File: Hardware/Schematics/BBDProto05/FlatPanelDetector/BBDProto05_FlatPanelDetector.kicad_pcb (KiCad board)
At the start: 2 copper layers, 170 x 110 mm, 124 parts, among them P01-01A1 VIA_06MM, P01-01B1 VIA_06MM, P01-02A1 VIA_06MM, P01-02B1 VIA_06MM, P01-03A1 VIA_06MM, P01-03B1 VIA_06MM, P01-04A1 VIA_06MM, P01-04B1 VIA_06MM, P01-05A1 VIA_06MM, P01-05B1 VIA_06MM, P01-06A1 VIA_06MM, P01-06B1 VIA_06MM, P02-01A1 VIA_06MM, P02-01B1 VIA_06MM, P02-02A1 VIA_06MM, P02-02B1 VIA_06MM, P02-03A1 VIA_06MM, P02-03B1 VIA_06MM, P02-04A1 VIA_06MM, P02-04B1 VIA_06MM, P02-05A1 VIA_06MM, P02-05B1 VIA_06MM, P02-06A1 VIA_06MM, P02-06B1 VIA_06MM, P03-01A1 VIA_06MM, P03-01B1 VIA_06MM, P03-02A1 VIA_06MM, P03-02B1 VIA_06MM, P03-03A1 VIA_06MM, P03-03B1 VIA_06MM, P03-04A1 VIA_06MM, P03-04B1 VIA_06MM, P03-05A1 VIA_06MM, P03-05B1 VIA_06MM, P03-06A1 VIA_06MM, P03-06B1 VIA_06MM, P04-01A1 VIA_06MM, P04-01B1 VIA_06MM, P04-02A1 VIA_06MM, P04-02B1 VIA_06MM, P04-03A1 VIA_06MM, P04-03B1 VIA_06MM, P04-04A1 VIA_06MM, P04-04B1 VIA_06MM, P04-05A1 VIA_06MM, P04-05B1 VIA_06MM, P04-06A1 VIA_06MM, P04-06B1 VIA_06MM, P05-01A1 VIA_06MM, P05-01B1 VIA_06MM, P05-02A1 VIA_06MM, P05-02B1 VIA_06MM, P05-03A1 VIA_06MM, P05-03B1 VIA_06MM, P05-04A1 VIA_06MM, P05-04B1 VIA_06MM, P05-05A1 VIA_06MM, P05-05B1 VIA_06MM, P05-06A1 VIA_06MM, P05-06B1 VIA_06MM, P06-01A1 VIA_06MM, P06-01B1 VIA_06MM, P06-02A1 VIA_06MM, P06-02B1 VIA_06MM, P06-03A1 VIA_06MM, P06-03B1 VIA_06MM, P06-04A1 VIA_06MM, P06-04B1 VIA_06MM, P06-05A1 VIA_06MM, P06-05B1 VIA_06MM, P06-06A1 VIA_06MM, P06-06B1 VIA_06MM, P07-01A1 VIA_06MM, P07-01B1 VIA_06MM, P07-02A1 VIA_06MM, P07-02B1 VIA_06MM, P07-03A1 VIA_06MM, P07-03B1 VIA_06MM, P07-04A1 VIA_06MM, P07-04B1 VIA_06MM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

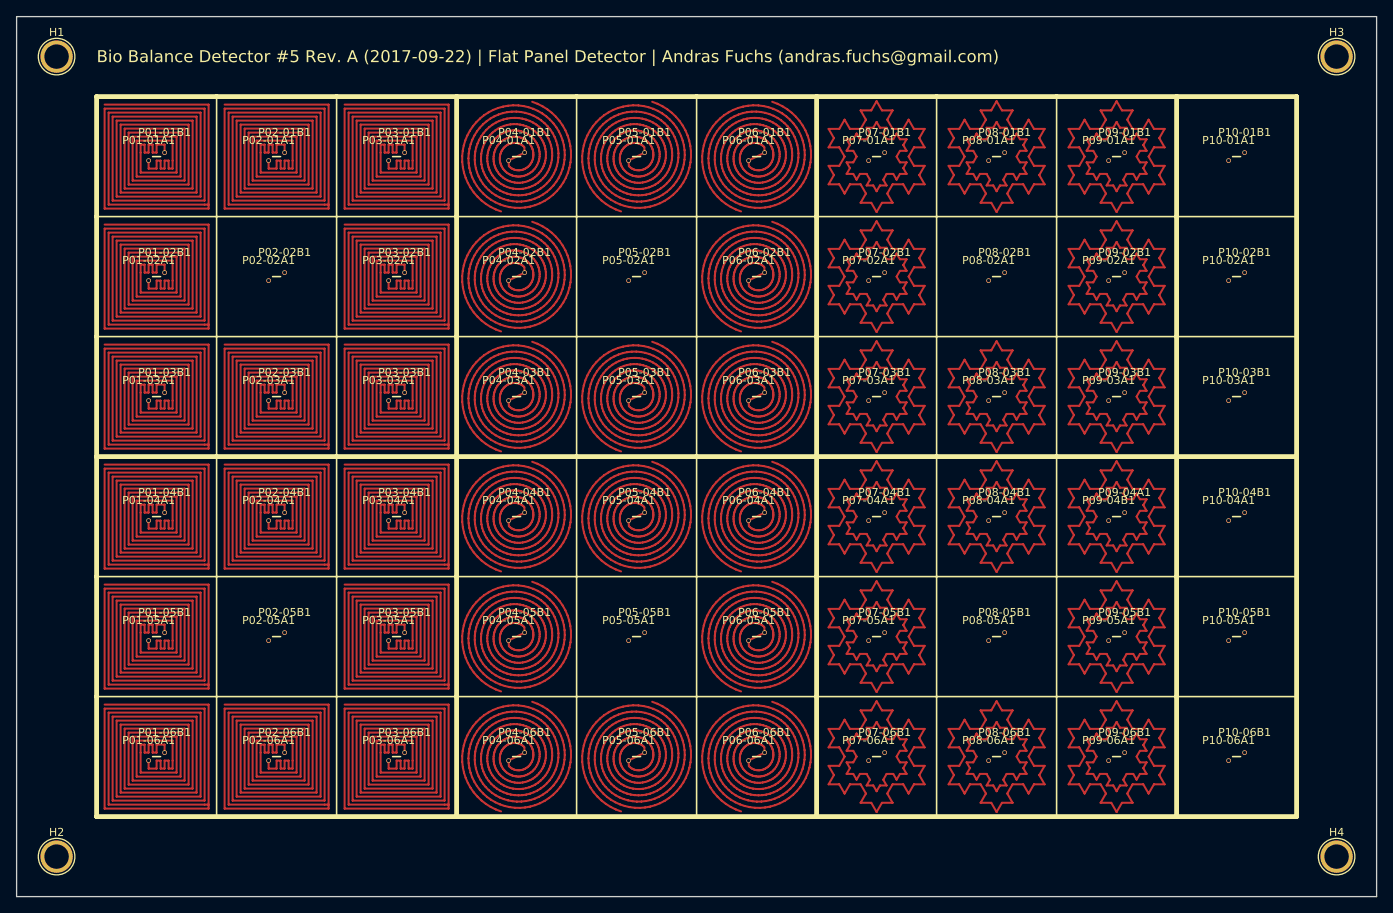
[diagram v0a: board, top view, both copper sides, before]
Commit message: FlatPanelDetector and its generator
FlatPanelDetector and its generator
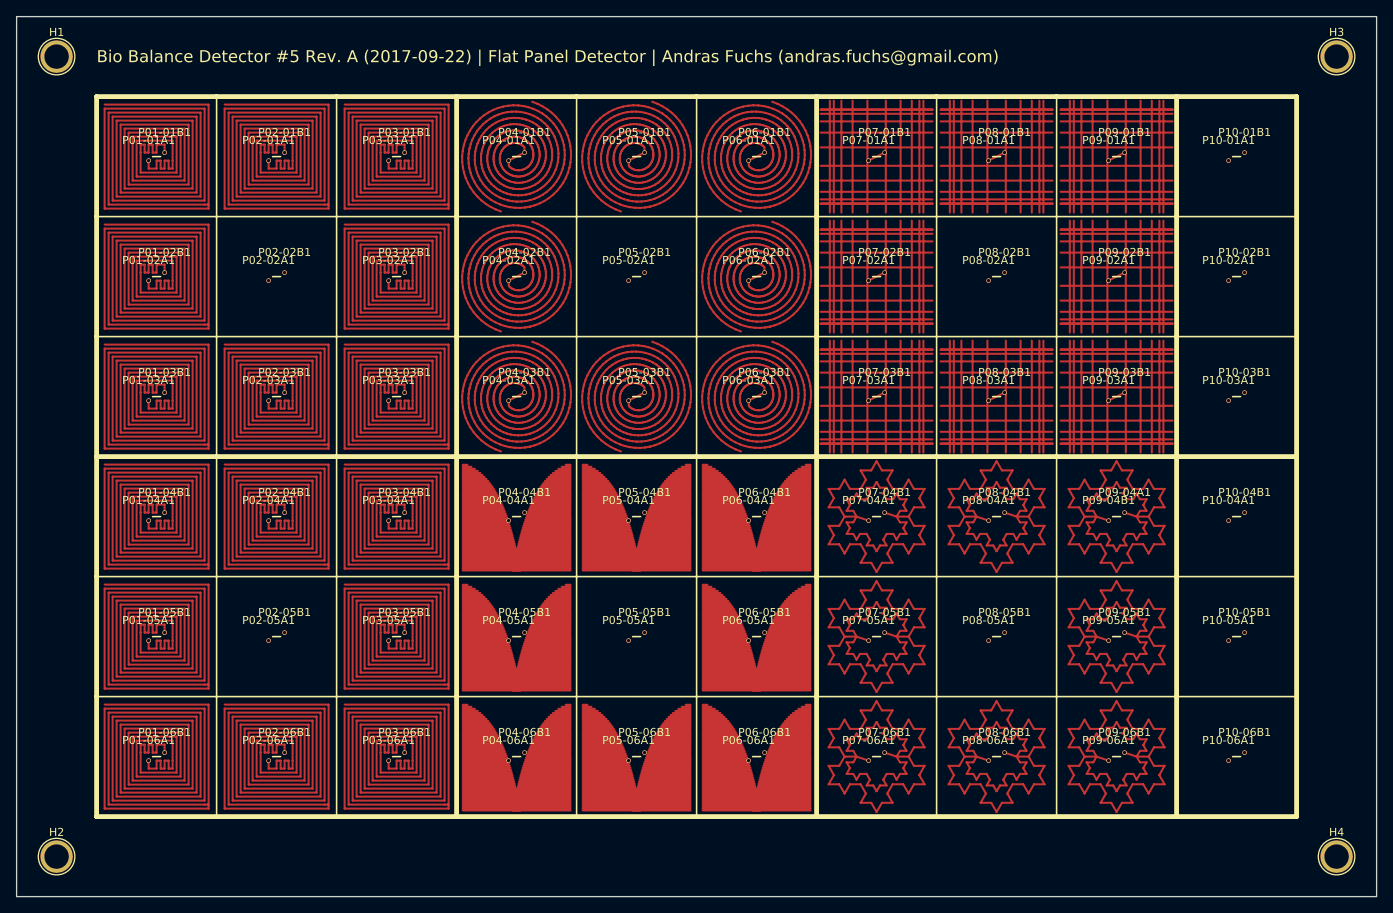
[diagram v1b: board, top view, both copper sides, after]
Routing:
- net (no net): track 1664.0 -> 6719.2 mm
- net Net-(P06-06A1-Pad1): track 197.7 -> 11.4 mm
- net Net-(P05-06A1-Pad1): track 197.7 -> 11.4 mm
- net Net-(P04-06A1-Pad1): track 197.7 -> 11.4 mm
- net Net-(P06-05A1-Pad1): track 197.7 -> 11.4 mm
- net Net-(P06-04A1-Pad1): track 197.7 -> 11.4 mm
- net Net-(P05-04A1-Pad1): track 197.7 -> 11.4 mm
- net Net-(P04-05A1-Pad1): track 197.7 -> 11.4 mm
- net Net-(P04-04A1-Pad1): track 197.7 -> 11.4 mm
- net Net-(P07-05A1-Pad1): track 0.00 -> 110.2 mm
- net Net-(P07-04A1-Pad1): track 0.00 -> 110.2 mm
- net Net-(P09-05A1-Pad1): track 0.00 -> 110.2 mm
- net Net-(P09-04A1-Pad1): track 0.00 -> 110.2 mm
- net Net-(P08-04A1-Pad1): track 0.00 -> 110.2 mm
- net Net-(P09-06A1-Pad1): track 0.00 -> 110.2 mm
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
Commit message: Fabrication files for the new flat panel detector
Fabrication files for the new flat panel detector
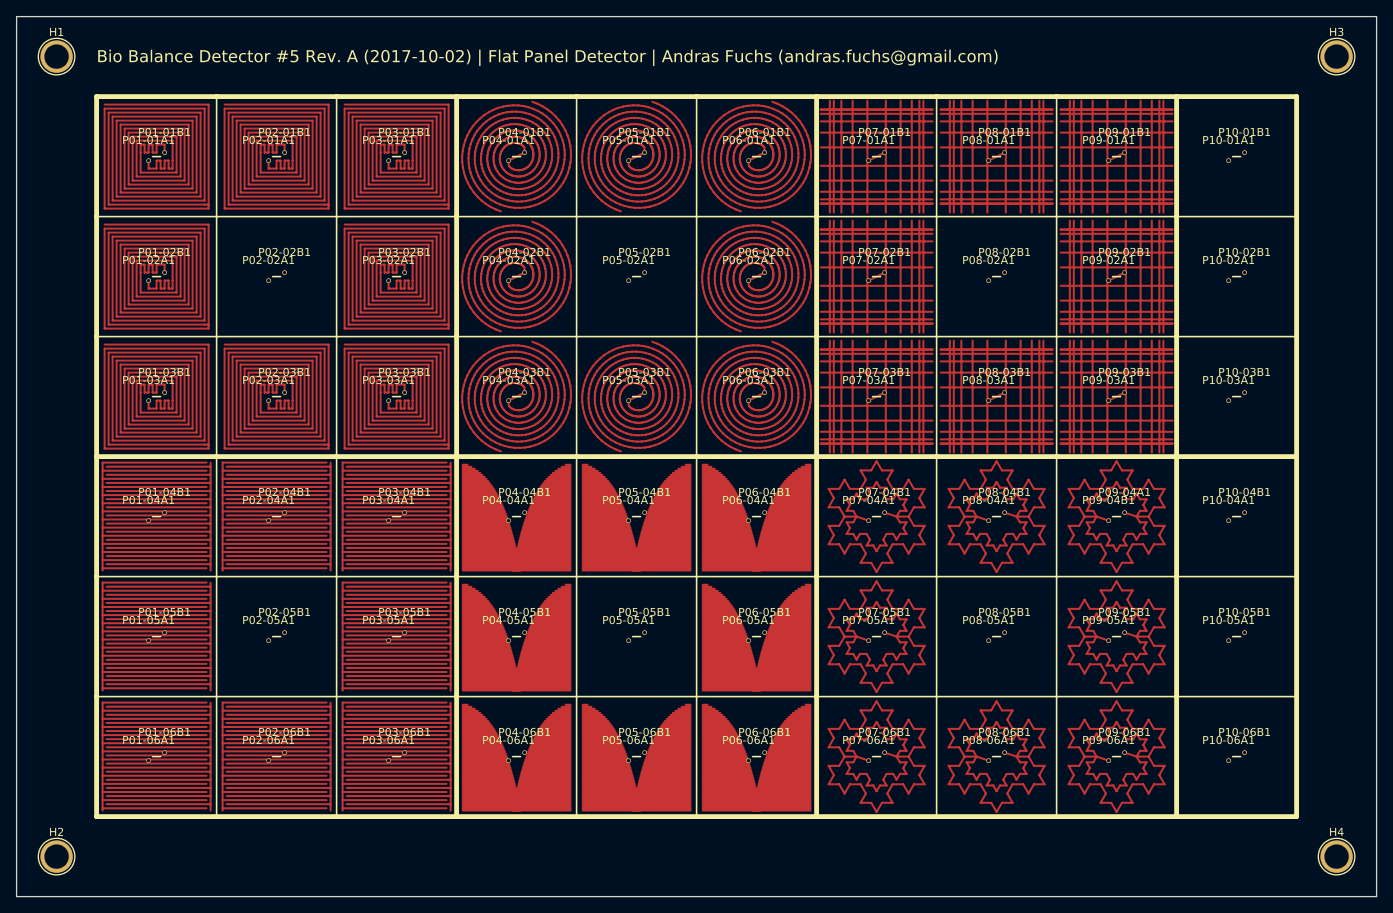
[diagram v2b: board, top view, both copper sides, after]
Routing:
- net (no net): track 6719.2 -> 9741.5 mm
- net Net-(P03-06A1-Pad1): track 355.5 -> 0.00 mm
- net Net-(P03-05A1-Pad1): track 355.5 -> 0.00 mm
- net Net-(P03-04A1-Pad1): track 355.5 -> 0.00 mm
- net Net-(P02-06A1-Pad1): track 355.5 -> 0.00 mm
- net Net-(P02-04A1-Pad1): track 355.5 -> 0.00 mm
- net Net-(P01-06A1-Pad1): track 355.5 -> 0.00 mm
- net Net-(P01-05A1-Pad1): track 355.5 -> 0.00 mm
- net Net-(P01-04A1-Pad1): track 355.5 -> 0.00 mm
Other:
- board text added: "Bio Balance Detector #5 Rev. A (2017-10-02) | Flat Panel Detector | Andras Fuchs (andras.fuchs@gmail.com)"
- board text removed: "Bio Balance Detector #5 Rev. A (2017-09-22) | Flat Panel Detector | Andras Fuchs (andras.fuchs@gmail.com)"
